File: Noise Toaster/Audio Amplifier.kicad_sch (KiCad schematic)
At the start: 13 parts, among them J1 AudioJack3_SwitchTR, U3 LM386

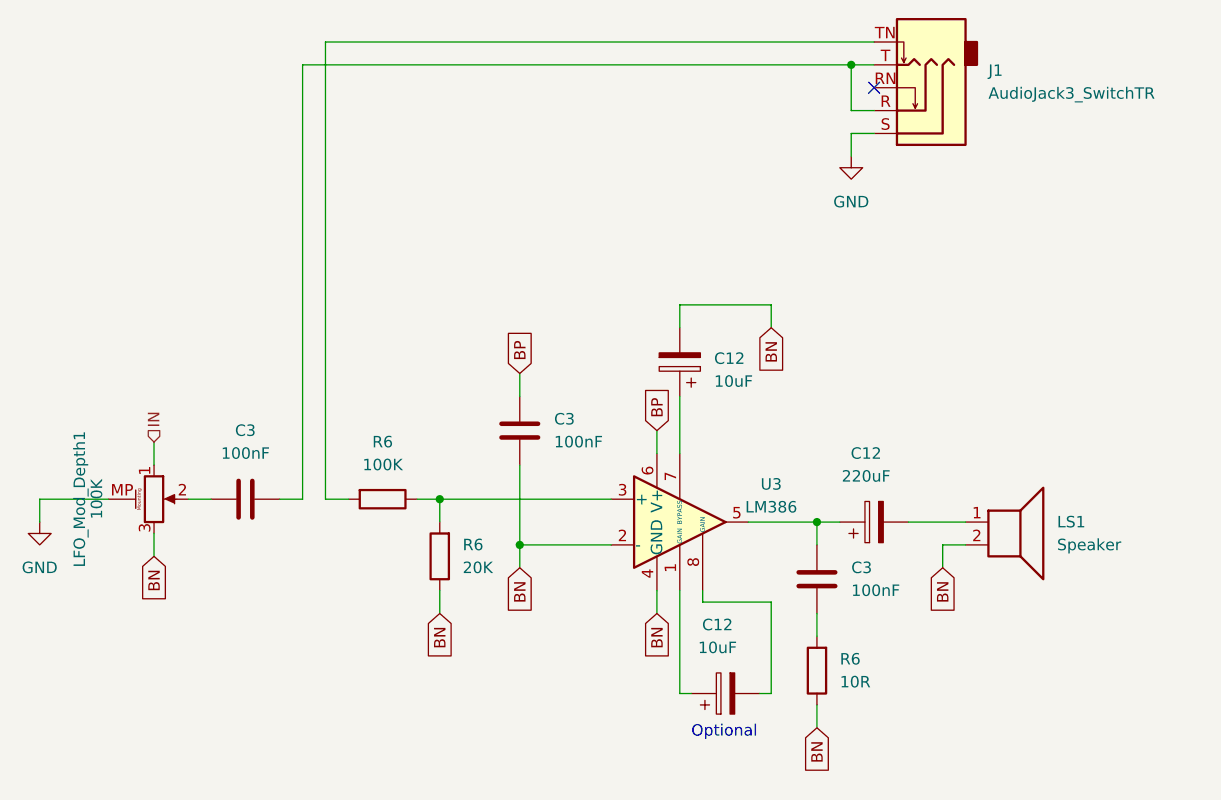
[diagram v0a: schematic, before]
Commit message: Noise Toaster - fixes after first board
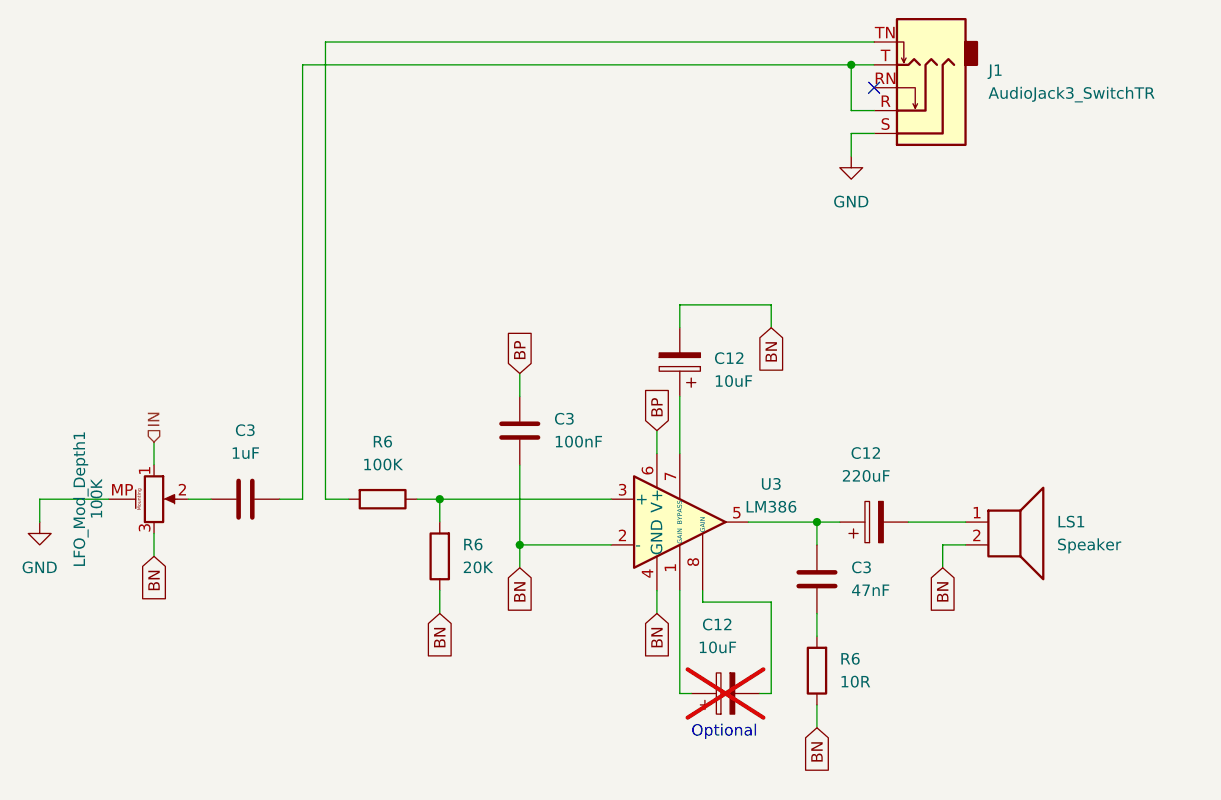
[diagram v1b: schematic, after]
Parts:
- C12: now not fitted; now left out of the parts list
- C3: value 100nF -> 1uF; footprint Capacitor_THT:C_Disc_D3.0mm_W2.0mm_P2.50mm -> Capacitor_THT:C_Radial_D5.0mm_H7.0mm_P2.00mm
- C3: value 100nF -> 47nF
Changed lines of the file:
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@@
       (effects (font (size 1.27 1.27)))
     )
-    (property "Value" "100nF" (at 88.9 104.14 90)
-      (effects (font (size 1.27 1.27)))
-    )
-    (property "Footprint" "Capacitor_THT:C_Disc_D3.0mm_W2.0mm_P2.50mm" (at 85.09 110.1852 0)
+    (property "Value" "1uF" (at 88.9 104.14 90)
+      (effects (font (size 1.27 1.27)))
+    )
+    (property "Footprint" "Capacitor_THT:C_Radial_D5.0mm_H7.0mm_P2.00mm" (at 85.09 110.1852 0)
       (effects (font (size 1.27 1.27)) hide)
     )
@@
       (effects (font (size 1.27 1.27)) (justify left))
     )
-    (property "Value" "100nF" (at 156.21 119.38 0)
+    (property "Value" "47nF" (at 156.21 119.38 0)
       (effects (font (size 1.27 1.27)) (justify left))
     )
@@
   )
   (symbol (lib_id "Device:C_Polarized") (at 142.24 130.81 90) (unit 1)
-    (in_bom yes) (on_board yes) (dnp no) (fields_autoplaced)
+    (in_bom no) (on_board yes) (dnp yes) (fields_autoplaced)
     (property "Reference" "C12" (at 141.351 123.19 90)
       (effects (font (size 1.27 1.27)))

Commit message: misc
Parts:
- renumbered C3 to C22, C3 to C23, C12 to C24, C12 to C25, C3 to C26, C12 to C27, R6 to R58, R6 to R59, R6 to R60, LFO_Mod_Depth1 to VOLUME1
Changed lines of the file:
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@@
   (symbol (lib_id "power:GND") (at 156.21 71.12 0) (unit 1)
     (in_bom yes) (on_board yes) (dnp no) (fields_autoplaced)
-    (property "Reference" "#PWR01" (at 156.21 77.47 0)
+    (property "Reference" "#PWR018" (at 156.21 77.47 0)
       (effects (font (size 1.27 1.27)) hide)
     )
@@
     (instances
       (project "Noise Toaster"
-        (path "/c06bdaff-9d92-4322-9a29-784b2d9ec2c6/3f36173e-f191-4036-853e-444de7299fbe"
-          (reference "#PWR01") (unit 1)
-        )
-        (path "/c06bdaff-9d92-4322-9a29-784b2d9ec2c6/3e542e49-c670-4cc9-bc62-1c16a197c718"
-          (reference "#PWR016") (unit 1)
-        )
         (path "/c06bdaff-9d92-4322-9a29-784b2d9ec2c6/70a61dae-82cc-4733-9246-2e61129addfb"
           (reference "#PWR018") (unit 1)
@@
   (symbol (lib_id "Device:C") (at 88.9 109.22 270) (unit 1)
     (in_bom yes) (on_board yes) (dnp no) (fields_autoplaced)
-    (property "Reference" "C3" (at 88.9 101.6 90)
+    (property "Reference" "C22" (at 88.9 101.6 90)
       (effects (font (size 1.27 1.27)))
     )
@@
     (instances
       (project "Noise Toaster"
-        (path "/c06bdaff-9d92-4322-9a29-784b2d9ec2c6/3f36173e-f191-4036-853e-444de7299fbe"
-          (reference "C3") (unit 1)
-        )
-        (path "/c06bdaff-9d92-4322-9a29-784b2d9ec2c6/74bc29e1-6bfb-4a22-9659-b607bacf38d2"
-          (reference "C19") (unit 1)
-        )
         (path "/c06bdaff-9d92-4322-9a29-784b2d9ec2c6/70a61dae-82cc-4733-9246-2e61129addfb"
           (reference "C22") (unit 1)
@@
   (symbol (lib_id "Device:C") (at 152.4 118.11 0) (unit 1)
     (in_bom yes) (on_board yes) (dnp no) (fields_autoplaced)
-    (property "Reference" "C3" (at 156.21 116.84 0)
+    (property "Reference" "C26" (at 156.21 116.84 0)
       (effects (font (size 1.27 1.27)) (justify left))
     )
@@
     (instances
       (project "Noise Toaster"
-        (path "/c06bdaff-9d92-4322-9a29-784b2d9ec2c6/3f36173e-f191-4036-853e-444de7299fbe"
-          (reference "C3") (unit 1)
-        )
-        (path "/c06bdaff-9d92-4322-9a29-784b2d9ec2c6/74bc29e1-6bfb-4a22-9659-b607bacf38d2"
-          (reference "C19") (unit 1)
-        )
         (path "/c06bdaff-9d92-4322-9a29-784b2d9ec2c6/70a61dae-82cc-4733-9246-2e61129addfb"
           (reference "C26") (unit 1)
@@
   (symbol (lib_id "power:GND") (at 66.04 111.76 0) (unit 1)
     (in_bom yes) (on_board yes) (dnp no) (fields_autoplaced)
-    (property "Reference" "#PWR01" (at 66.04 118.11 0)
+    (property "Reference" "#PWR017" (at 66.04 118.11 0)
       (effects (font (size 1.27 1.27)) hide)
     )
@@
     (instances
       (project "Noise Toaster"
-        (path "/c06bdaff-9d92-4322-9a29-784b2d9ec2c6/3f36173e-f191-4036-853e-444de7299fbe"
-          (reference "#PWR01") (unit 1)
-        )
-        (path "/c06bdaff-9d92-4322-9a29-784b2d9ec2c6/3e542e49-c670-4cc9-bc62-1c16a197c718"
-          (reference "#PWR016") (unit 1)
-        )
         (path "/c06bdaff-9d92-4322-9a29-784b2d9ec2c6/70a61dae-82cc-4733-9246-2e61129addfb"
           (reference "#PWR017") (unit 1)
@@
   (symbol (lib_id "Device:R") (at 110.49 115.57 180) (unit 1)
     (in_bom yes) (on_board yes) (dnp no) (fields_autoplaced)
-    (property "Reference" "R6" (at 113.03 114.3 0)
+    (property "Reference" "R59" (at 113.03 114.3 0)
       (effects (font (size 1.27 1.27)) (justify right))
     )
@@
     (instances
       (project "Noise Toaster"
-        (path "/c06bdaff-9d92-4322-9a29-784b2d9ec2c6/3f36173e-f191-4036-853e-444de7299fbe"
-          (reference "R6") (unit 1)
-        )
-        (path "/c06bdaff-9d92-4322-9a29-784b2d9ec2c6/3e542e49-c670-4cc9-bc62-1c16a197c718"
-          (reference "R54") (unit 1)
-        )
         (path "/c06bdaff-9d92-4322-9a29-784b2d9ec2c6/70a61dae-82cc-4733-9246-2e61129addfb"
           (reference "R59") (unit 1)
@@
   (symbol (lib_id "Device:C_Polarized") (at 142.24 130.81 90) (unit 1)
     (in_bom no) (on_board yes) (dnp yes) (fields_autoplaced)
-    (property "Reference" "C12" (at 141.351 123.19 90)
+    (property "Reference" "C25" (at 141.351 123.19 90)
       (effects (font (size 1.27 1.27)))
     )
@@
     (instances
       (project "Noise Toaster"
-        (path "/c06bdaff-9d92-4322-9a29-784b2d9ec2c6/46712425-f81c-4e59-b8d1-7e996aa9ca64"
-          (reference "C12") (unit 1)
-        )
-        (path "/c06bdaff-9d92-4322-9a29-784b2d9ec2c6/74bc29e1-6bfb-4a22-9659-b607bacf38d2"
-          (reference "C20") (unit 1)
-        )
         (path "/c06bdaff-9d92-4322-9a29-784b2d9ec2c6/70a61dae-82cc-4733-9246-2e61129addfb"
           (reference "C25") (unit 1)
@@
   (symbol (lib_id "Device:R") (at 152.4 128.27 180) (unit 1)
     (in_bom yes) (on_board yes) (dnp no) (fields_autoplaced)
-    (property "Reference" "R6" (at 154.94 127 0)
+    (property "Reference" "R60" (at 154.94 127 0)
       (effects (font (size 1.27 1.27)) (justify right))
     )
@@
     (instances
       (project "Noise Toaster"
-        (path "/c06bdaff-9d92-4322-9a29-784b2d9ec2c6/3f36173e-f191-4036-853e-444de7299fbe"
-          (reference "R6") (unit 1)
-        )
-        (path "/c06bdaff-9d92-4322-9a29-784b2d9ec2c6/3e542e49-c670-4cc9-bc62-1c16a197c718"
-          (reference "R54") (unit 1)
-        )
         (path "/c06bdaff-9d92-4322-9a29-784b2d9ec2c6/70a61dae-82cc-4733-9246-2e61129addfb"
           (reference "R60") (unit 1)
@@
   (symbol (lib_id "Device:C_Polarized") (at 137.16 93.98 180) (unit 1)
     (in_bom yes) (on_board yes) (dnp no) (fields_autoplaced)
-    (property "Reference" "C12" (at 140.97 93.599 0)
+    (property "Reference" "C24" (at 140.97 93.599 0)
       (effects (font (size 1.27 1.27)) (justify right))
     )
@@
     (instances
       (project "Noise Toaster"
-        (path "/c06bdaff-9d92-4322-9a29-784b2d9ec2c6/46712425-f81c-4e59-b8d1-7e996aa9ca64"
-          (reference "C12") (unit 1)
-        )
-        (path "/c06bdaff-9d92-4322-9a29-784b2d9ec2c6/74bc29e1-6bfb-4a22-9659-b607bacf38d2"
-          (reference "C20") (unit 1)
-        )
         (path "/c06bdaff-9d92-4322-9a29-784b2d9ec2c6/70a61dae-82cc-4733-9246-2e61129addfb"
           (reference "C24") (unit 1)
@@
   (symbol (lib_id "Device:R") (at 104.14 109.22 270) (unit 1)
     (in_bom yes) (on_board yes) (dnp no) (fields_autoplaced)
-    (property "Reference" "R6" (at 104.14 102.87 90)
+    (property "Reference" "R58" (at 104.14 102.87 90)
       (effects (font (size 1.27 1.27)))
     )
@@
     (instances
       (project "Noise Toaster"
-        (path "/c06bdaff-9d92-4322-9a29-784b2d9ec2c6/3f36173e-f191-4036-853e-444de7299fbe"
-          (reference "R6") (unit 1)
-        )
-        (path "/c06bdaff-9d92-4322-9a29-784b2d9ec2c6/3e542e49-c670-4cc9-bc62-1c16a197c718"
-          (reference "R54") (unit 1)
-        )
         (path "/c06bdaff-9d92-4322-9a29-784b2d9ec2c6/70a61dae-82cc-4733-9246-2e61129addfb"
           (reference "R58") (unit 1)
@@
   (symbol (lib_id "Device:R_Potentiometer_MountingPin") (at 78.74 109.22 0) (unit 1)
     (in_bom yes) (on_board yes) (dnp no)
-    (property "Reference" "LFO_Mod_Depth1" (at 70.485 109.22 90)
+    (property "Reference" "VOLUME1" (at 70.485 109.22 90)
       (effects (font (size 1.27 1.27)))
     )
@@
     (instances
       (project "Noise Toaster"
-        (path "/c06bdaff-9d92-4322-9a29-784b2d9ec2c6/3f36173e-f191-4036-853e-444de7299fbe"
-          (reference "LFO_Mod_Depth1") (unit 1)
-        )
-        (path "/c06bdaff-9d92-4322-9a29-784b2d9ec2c6/74bc29e1-6bfb-4a22-9659-b607bacf38d2"
-          (reference "LFO_RATE1") (unit 1)
-        )
-        (path "/c06bdaff-9d92-4322-9a29-784b2d9ec2c6/3e542e49-c670-4cc9-bc62-1c16a197c718"
-          (reference "RELEASE_TIME1") (unit 1)
-        )
         (path "/c06bdaff-9d92-4322-9a29-784b2d9ec2c6/70a61dae-82cc-4733-9246-2e61129addfb"
           (reference "VOLUME1") (unit 1)
@@
   (symbol (lib_id "Device:C_Polarized") (at 158.75 111.76 90) (unit 1)
     (in_bom yes) (on_board yes) (dnp no) (fields_autoplaced)
-    (property "Reference" "C12" (at 157.861 104.14 90)
+    (property "Reference" "C27" (at 157.861 104.14 90)
       (effects (font (size 1.27 1.27)))
     )
@@
     (instances
       (project "Noise Toaster"
-        (path "/c06bdaff-9d92-4322-9a29-784b2d9ec2c6/46712425-f81c-4e59-b8d1-7e996aa9ca64"
-          (reference "C12") (unit 1)
-        )
-        (path "/c06bdaff-9d92-4322-9a29-784b2d9ec2c6/74bc29e1-6bfb-4a22-9659-b607bacf38d2"
-          (reference "C20") (unit 1)
-        )
         (path "/c06bdaff-9d92-4322-9a29-784b2d9ec2c6/70a61dae-82cc-4733-9246-2e61129addfb"
           (reference "C27") (unit 1)
@@
   (symbol (lib_id "Device:C") (at 119.38 101.6 0) (unit 1)
     (in_bom yes) (on_board yes) (dnp no) (fields_autoplaced)
-    (property "Reference" "C3" (at 123.19 100.33 0)
+    (property "Reference" "C23" (at 123.19 100.33 0)
       (effects (font (size 1.27 1.27)) (justify left))
     )
@@
     (instances
       (project "Noise Toaster"
-        (path "/c06bdaff-9d92-4322-9a29-784b2d9ec2c6/3f36173e-f191-4036-853e-444de7299fbe"
-          (reference "C3") (unit 1)
-        )
-        (path "/c06bdaff-9d92-4322-9a29-784b2d9ec2c6/74bc29e1-6bfb-4a22-9659-b607bacf38d2"
-          (reference "C19") (unit 1)
-        )
         (path "/c06bdaff-9d92-4322-9a29-784b2d9ec2c6/70a61dae-82cc-4733-9246-2e61129addfb"
           (reference "C23") (unit 1)
